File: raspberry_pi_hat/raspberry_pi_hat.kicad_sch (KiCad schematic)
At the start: 14 parts, among them IC1 LM3940IT, J1 GPIO, J5 LCD_screeen, J6 GPIO, J7 Switches, J8 LED_status, U3 NRF24L01P

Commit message: Adding USB power connector
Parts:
- added J2: USB_C_Receptacle_PowerOnly_6P, Connector_USB:USB_C_Receptacle_GCT_USB4125-xx-x-0190_6P_TopMnt_Horizontal, symbol Connector:USB_C_Receptacle_PowerOnly_6P
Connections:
- new net: J2.A12 (GND), J2.B12 (GND)
- new net: J2.A9 (VBUS), J2.B9 (VBUS)
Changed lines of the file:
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@@
+		)
+	)
+	(symbol
+		(lib_id "Connector:USB_C_Receptacle_PowerOnly_6P")
+		(at 205.74 133.35 0)
+		(unit 1)
+		(exclude_from_sim no)
+		(in_bom yes)
+		(on_board yes)
+		(dnp no)
+		(fields_autoplaced yes)
+		(property "Reference" "J2"
+			(at 205.74 115.57 0)
+			(effects
+				(font
+					(size 1.27 1.27)
+				)
+			)
+		)
+		(property "Value" "USB_C_Receptacle_PowerOnly_6P"
+			(at 205.74 118.11 0)
+			(effects
+				(font
+					(size 1.27 1.27)
+				)
+			)
+		)
+		(property "Footprint" "Connector_USB:USB_C_Receptacle_GCT_USB4125-xx-x-0190_6P_TopMnt_Horizontal"
+			(at 209.55 130.81 0)
+			(effects
+				(font
+					(size 1.27 1.27)
+				)
+				(hide yes)
+			)
+		)
+		(property "Datasheet" "https://www.usb.org/sites/default/files/documents/usb_type-c.zip"
+			(at 205.74 133.35 0)
+			(effects
+				(font
+					(size 1.27 1.27)
+				)
+				(hide yes)
+			)
+		)
+		(property "Description" "USB Power-Only 6P Type-C Receptacle connector"
+			(at 205.74 133.35 0)
+			(effects
+				(font
+					(size 1.27 1.27)
+				)
+				(hide yes)
+			)
+		)
+		(pin "B12"
+		)
+		(pin "B9"
+		)
+		(pin "B5"
+		)
+		(pin "A5"
+		)
+		(pin "A12"
+		)
+		(pin "A9"
+		)
+		(pin "S1"
+		)
+		(instances
+			(project ""
+				(path "/e63e39d7-6ac0-4ffd-8aa3-1841a4541b55"
+					(reference "J2")
+					(unit 1)
+				)
+			)
 		)
 	)

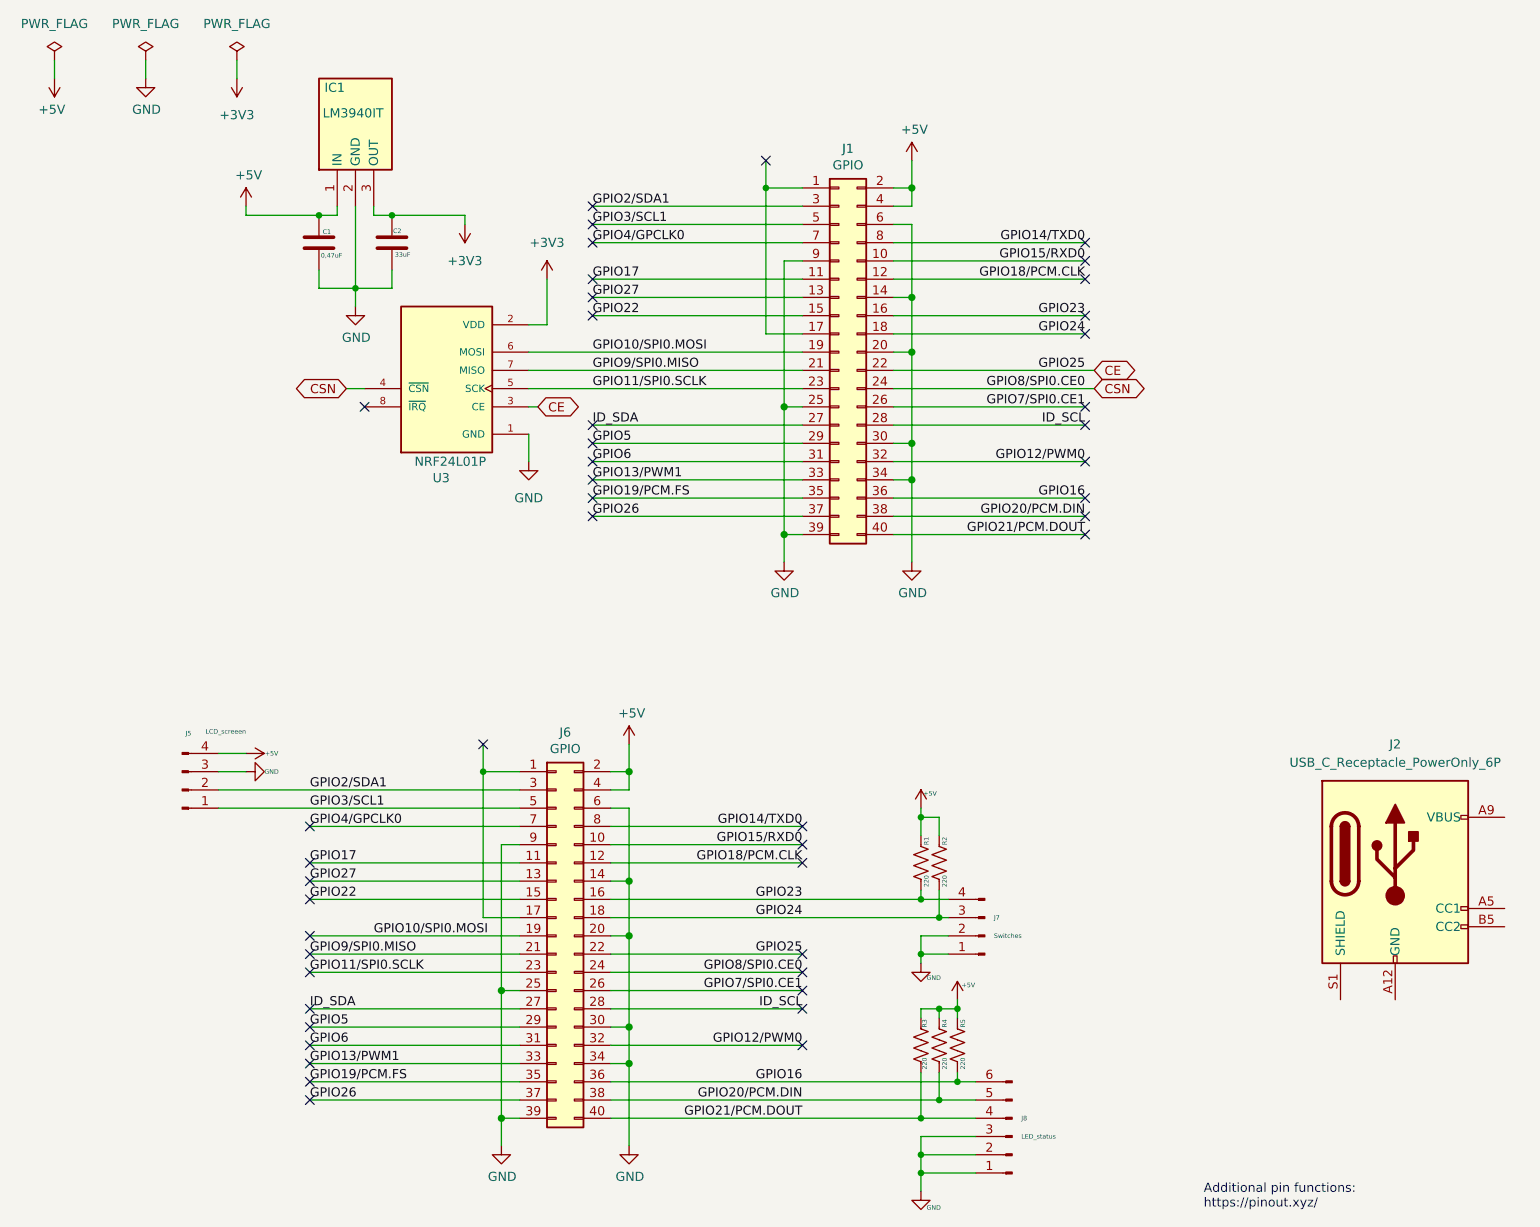
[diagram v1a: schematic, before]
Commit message: improving schematics to fit layout requirements
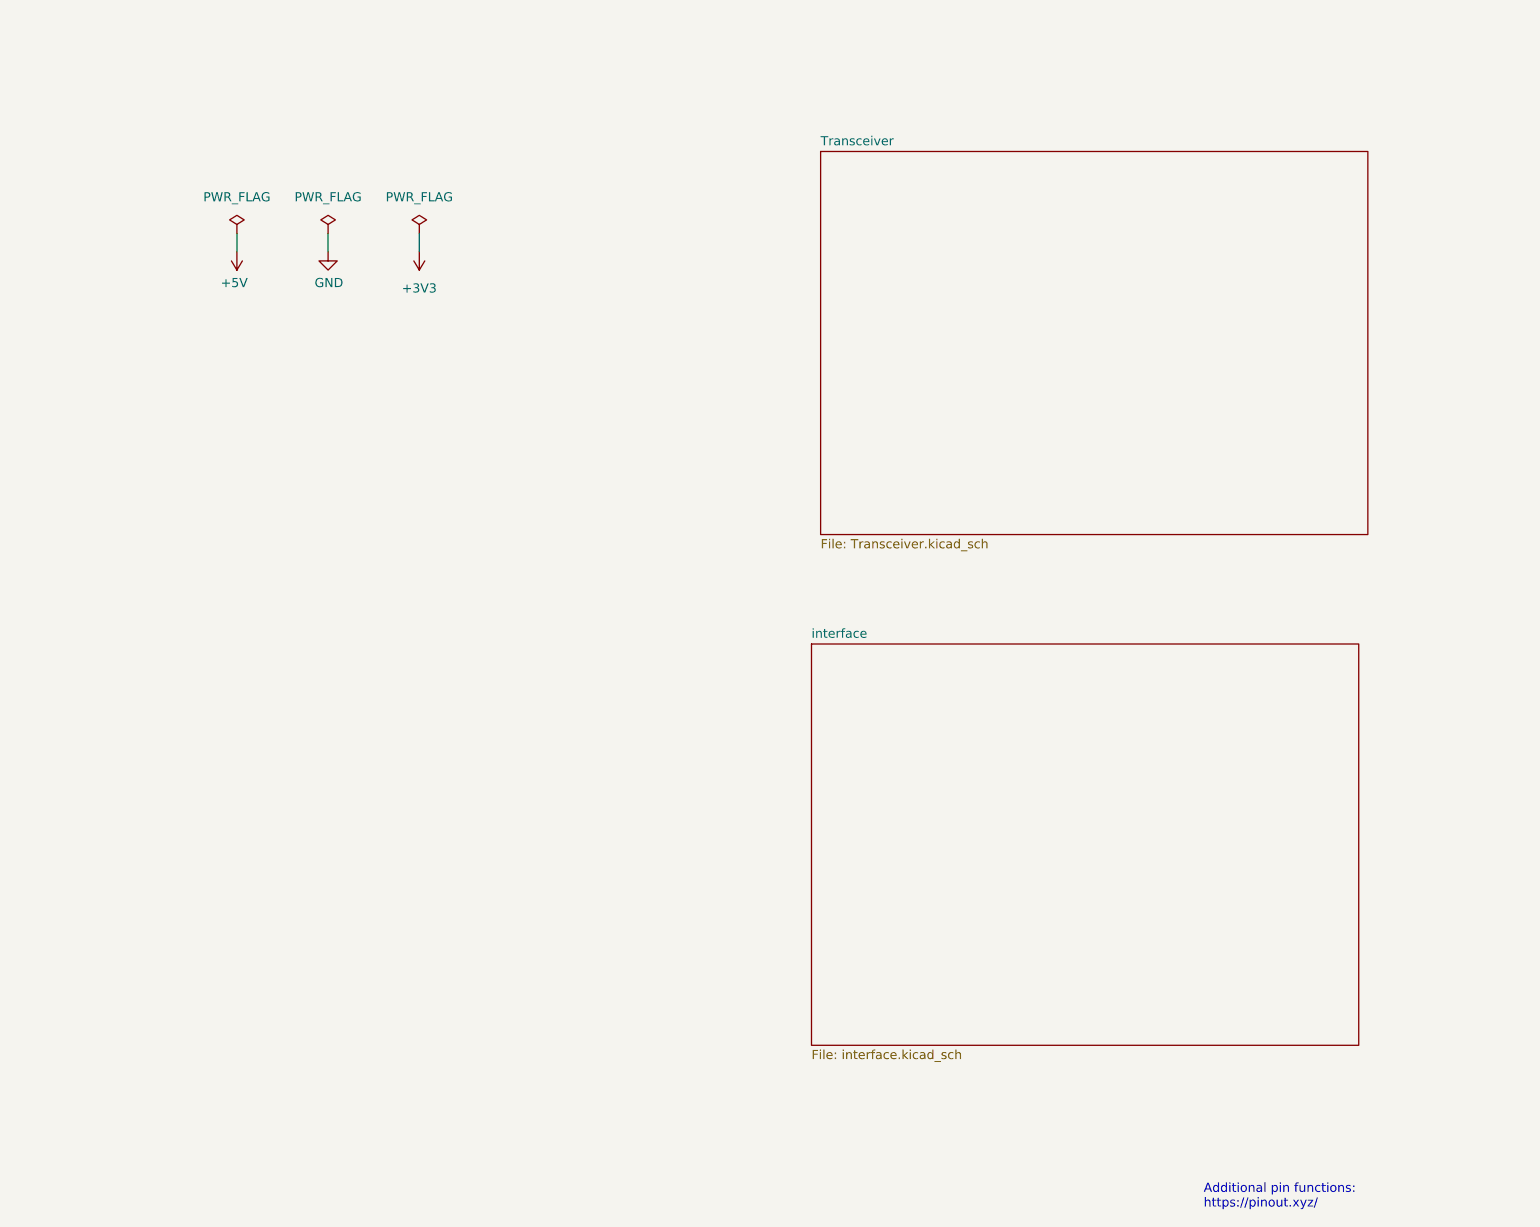
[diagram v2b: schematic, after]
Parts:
- removed C1: 0,47uF, Capacitor_THT:C_Radial_D4.0mm_H5.0mm_P1.50mm, symbol Device:C
- removed C2: 33uF, Capacitor_THT:C_Radial_D4.0mm_H5.0mm_P1.50mm, symbol Device:C
- removed IC1: LM3940IT, Package_TO_SOT_THT:TO-262-3-1EP_Horizontal_TabDown, symbol LM3940IT-3_3-NOPB:LM3940IT-3.3_NOPB
- removed J1, J6: GPIO, Module:Raspberry_Pi_Zero_Socketed_THT_FaceDown_MountingHoles, symbol Connector_Generic:Conn_02x20_Odd_Even
- removed J2: USB_C_Receptacle_PowerOnly_6P, Connector_USB:USB_C_Receptacle_GCT_USB4125-xx-x-0190_6P_TopMnt_Horizontal, symbol Connector:USB_C_Receptacle_PowerOnly_6P
- removed J5: LCD_screeen, Connector_Molex:Molex_KK-254_AE-6410-04A_1x04_P2.54mm_Vertical, symbol Connector:Conn_01x04_Pin
- removed J7: Switches, Connector_Molex:Molex_KK-254_AE-6410-04A_1x04_P2.54mm_Vertical, symbol Connector:Conn_01x04_Pin
- removed J8: LED_status, Connector_Molex:Molex_KK-254_AE-6410-06A_1x06_P2.54mm_Vertical, symbol Connector:Conn_01x06_Pin
- removed R1, R2, R3, R4, R5: 220, Resistor_THT:R_Axial_DIN0309_L9.0mm_D3.2mm_P12.70mm_Horizontal, symbol Device:R_US
- removed U3: NRF24L01P, NRF24L01P-MODULE-PCB:XCVR_NRF24L01P-MODULE-PCB, symbol NRF24L01P-MODULE-PCB:NRF24L01P-MODULE-PCB
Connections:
- no-connect marks 47 -> 0
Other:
- added sheet Transceiver (Transceiver.kicad_sch)
- added sheet interface (interface.kicad_sch)

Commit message: Solved split connection issues between boards
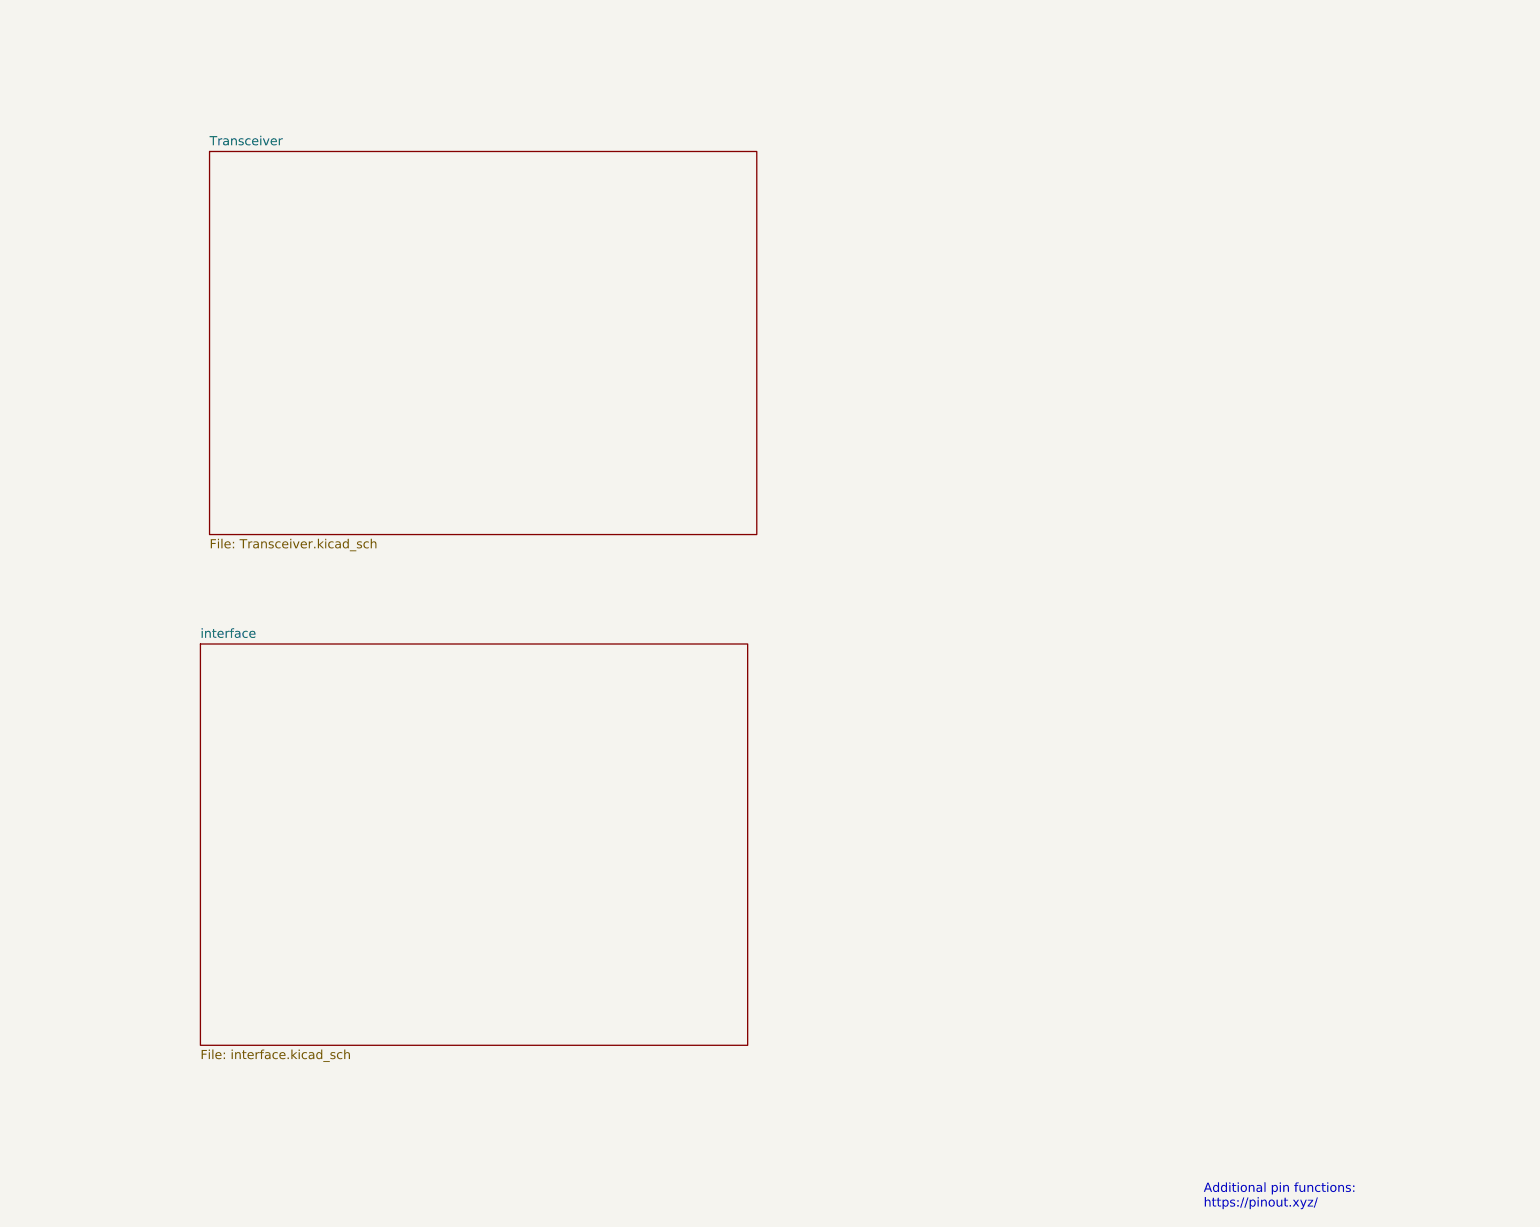
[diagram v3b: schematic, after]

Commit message: Combined both PCBs successfully and solved errors
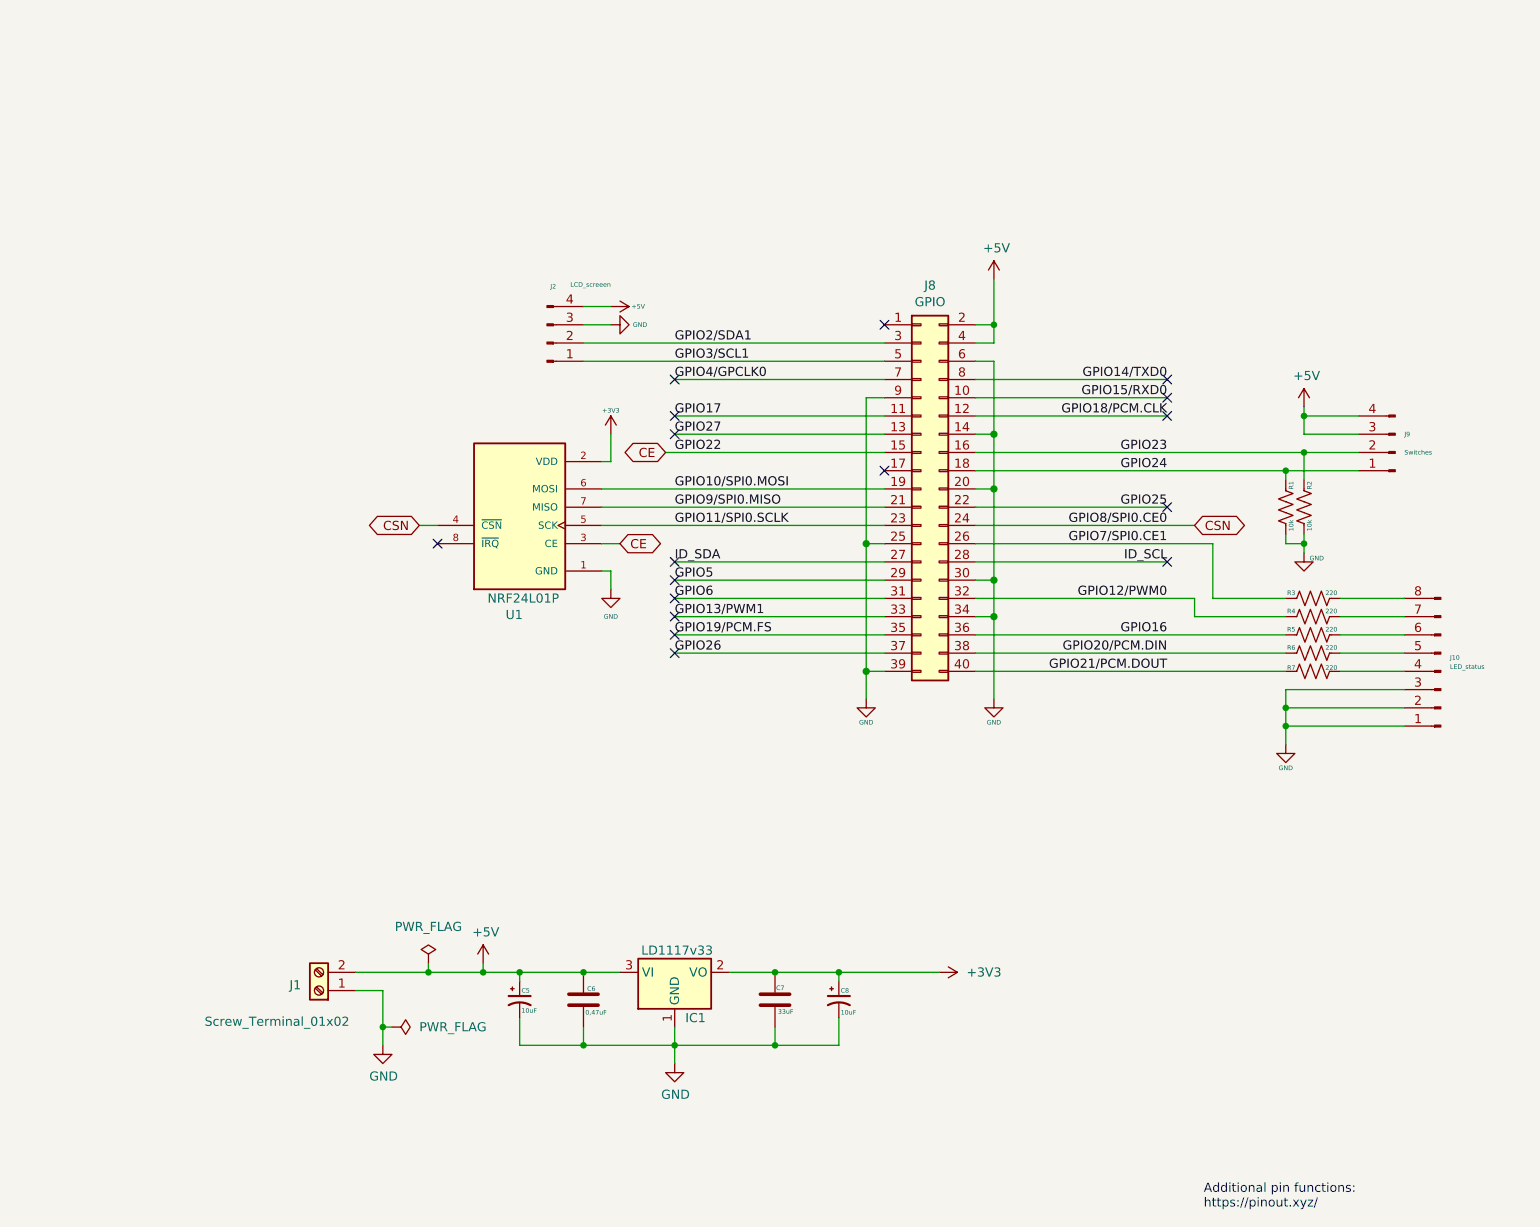
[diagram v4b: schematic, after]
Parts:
- added C5, C8: 10uF, Capacitor_THT:CP_Radial_D5.0mm_P2.50mm, symbol Device:C_Polarized_Small_US
- added C6: 0,47uF, Capacitor_THT:C_Radial_D4.0mm_H5.0mm_P1.50mm, symbol Device:C
- added C7: 33uF, Capacitor_THT:C_Radial_D4.0mm_H5.0mm_P1.50mm, symbol Device:C
- added IC1: LD1117v33, Package_TO_SOT_THT:TO-220-3_Vertical, symbol Regulator_Linear:LD1117S33TR_SOT223
- added J1: Screw_Terminal_01x02, TerminalBlock_MetzConnect:TerminalBlock_MetzConnect_Type101_RT01602HBWC_1x02_P5.08mm_Horizontal, symbol Connector:Screw_Terminal_01x02
- added J10: LED_status, Connector_Molex:Molex_KK-254_AE-6410-08A_1x08_P2.54mm_Vertical, symbol Connector:Conn_01x08_Pin
- added J2: LCD_screeen, Connector_Molex:Molex_KK-254_AE-6410-04A_1x04_P2.54mm_Vertical, symbol Connector:Conn_01x04_Pin
- added J8: GPIO, Module:Raspberry_Pi_Zero_Socketed_THT_FaceDown_MountingHoles, symbol Connector_Generic:Conn_02x20_Odd_Even
- added J9: Switches, Connector_Molex:Molex_KK-254_AE-6410-04A_1x04_P2.54mm_Vertical, symbol Connector:Conn_01x04_Pin
- added R1, R2: 10k, Resistor_THT:R_Axial_DIN0309_L9.0mm_D3.2mm_P12.70mm_Horizontal, symbol Device:R_US
- added R3, R4, R5, R6, R7: 220, Resistor_THT:R_Axial_DIN0309_L9.0mm_D3.2mm_P12.70mm_Horizontal, symbol Device:R_US
- added U1: NRF24L01P, NRF24L01P-MODULE-PCB:XCVR_NRF24L01P-MODULE-PCB, symbol NRF24L01P-MODULE-PCB:NRF24L01P-MODULE-PCB
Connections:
- new net: J10.8 (Pin_8), R3.2
- new net: J10.6 (Pin_6), R5.2
- new net: J10.4 (Pin_4), R7.2
- new net: J10.7 (Pin_7), R4.2
- new net: J10.5 (Pin_5), R6.2
- new net +3V3: C7.1, C8.1, IC1.2 (VO), U1.2 (VDD)
- new net +5V: C5.1, C6.1, IC1.3 (VI), J1.2 (Pin_2), J2.4 (Pin_4), J8.2 (Pin_2), J8.4 (Pin_4), J9.3 (Pin_3), J9.4 (Pin_4)
- new net CE: J8.15 (Pin_15), U1.3 (CE)
- new net CSN: J8.24 (Pin_24), U1.4 (~{CSN})
- new net GND: C5.2, C6.2, C7.2, C8.2, IC1.1 (GND), J1.1 (Pin_1), J10.1 (Pin_1), J10.2 (Pin_2), J10.3 (Pin_3), J2.3 (Pin_3), J8.14 (Pin_14), J8.20 (Pin_20), J8.25 (Pin_25), J8.30 (Pin_30), J8.34 (Pin_34), J8.39 (Pin_39), J8.6 (Pin_6), J8.9 (Pin_9), R1.2, R2.2, U1.1 (GND)
- new net GPIO10/SPI0.MOSI: J8.19 (Pin_19), U1.6 (MOSI)
- new net GPIO11/SPI0.SCLK: J8.23 (Pin_23), U1.5 (SCK)
- new net GPIO12/PWM0: J8.32 (Pin_32), R4.1
- new net GPIO13/PWM1: J8.33 (Pin_33)
- new net GPIO14/TXD0: J8.8 (Pin_8)
- new net GPIO15/RXD0: J8.10 (Pin_10)
- new net GPIO16: J8.36 (Pin_36), R5.1
- new net GPIO17: J8.11 (Pin_11)
- new net GPIO18/PCM.CLK: J8.12 (Pin_12)
- new net GPIO19/PCM.FS: J8.35 (Pin_35)
- new net GPIO20/PCM.DIN: J8.38 (Pin_38), R6.1
- new net GPIO21/PCM.DOUT: J8.40 (Pin_40), R7.1
- new net GPIO23: J8.16 (Pin_16), J9.2 (Pin_2), R2.1
- new net GPIO24: J8.18 (Pin_18), J9.1 (Pin_1), R1.1
- new net GPIO25: J8.22 (Pin_22)
- new net GPIO26: J8.37 (Pin_37)
- new net GPIO27: J8.13 (Pin_13)
- new net GPIO2/SDA1: J2.2 (Pin_2), J8.3 (Pin_3)
- new net GPIO3/SCL1: J2.1 (Pin_1), J8.5 (Pin_5)
- new net GPIO4/GPCLK0: J8.7 (Pin_7)
- new net GPIO5: J8.29 (Pin_29)
- new net GPIO6: J8.31 (Pin_31)
- new net GPIO7/SPI0.CE1: J8.26 (Pin_26), R3.1
- new net GPIO9/SPI0.MISO: J8.21 (Pin_21), U1.7 (MISO)
- new net ID_SCL: J8.28 (Pin_28)
- new net ID_SDA: J8.27 (Pin_27)
- no-connect marks 0 -> 17
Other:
- removed sheet Transceiver
- removed sheet interface

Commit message: improved final version
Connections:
- net GPIO27: now also U1.8 (~{IRQ})
- no-connect marks 17 -> 15
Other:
- moved on the sheet: C5, C6, C7, C8, IC1, J1
